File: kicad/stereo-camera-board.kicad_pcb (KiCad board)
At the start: 4 copper layers, 57 x 70 mm, 86 parts, among them IC1 ZLDO1117G33TA, IC2 MCP1700T-2502E/TT, IC3 SN74LVC1T45DCKR, IC4 SN74LVC1T45DCKR, IC5 SN74LVC1T45DCKR, T1 2n2222a, T2 2N2907A, U1 GSB311231HR, U2 ATXMEGA256A3-AU, U3 MAX3207E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

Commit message: Cleaned up module references for silk screen.
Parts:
- FSM4JSMA-SMD: renamed from Reset; value FSM4JSMA-SMD -> RESET
- JP3: value AVR-JTAG-10 -> JTAG
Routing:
- net N-0000067: track 14.9 -> 16.2 mm
- net (no net): track 1.19 -> 1.29 mm, vias 0 -> 109
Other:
- board text added: "+5V"
- board text added: "GND"

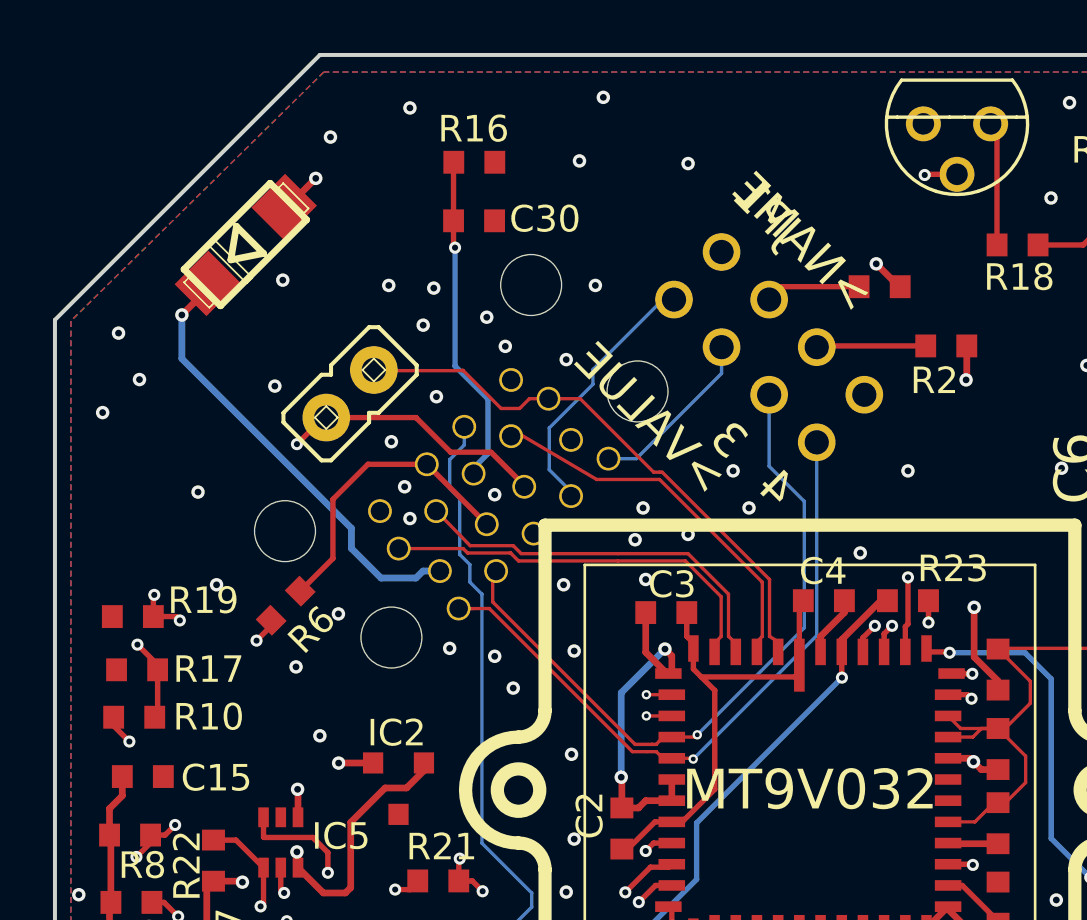
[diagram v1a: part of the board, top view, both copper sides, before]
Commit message: Modified usb module
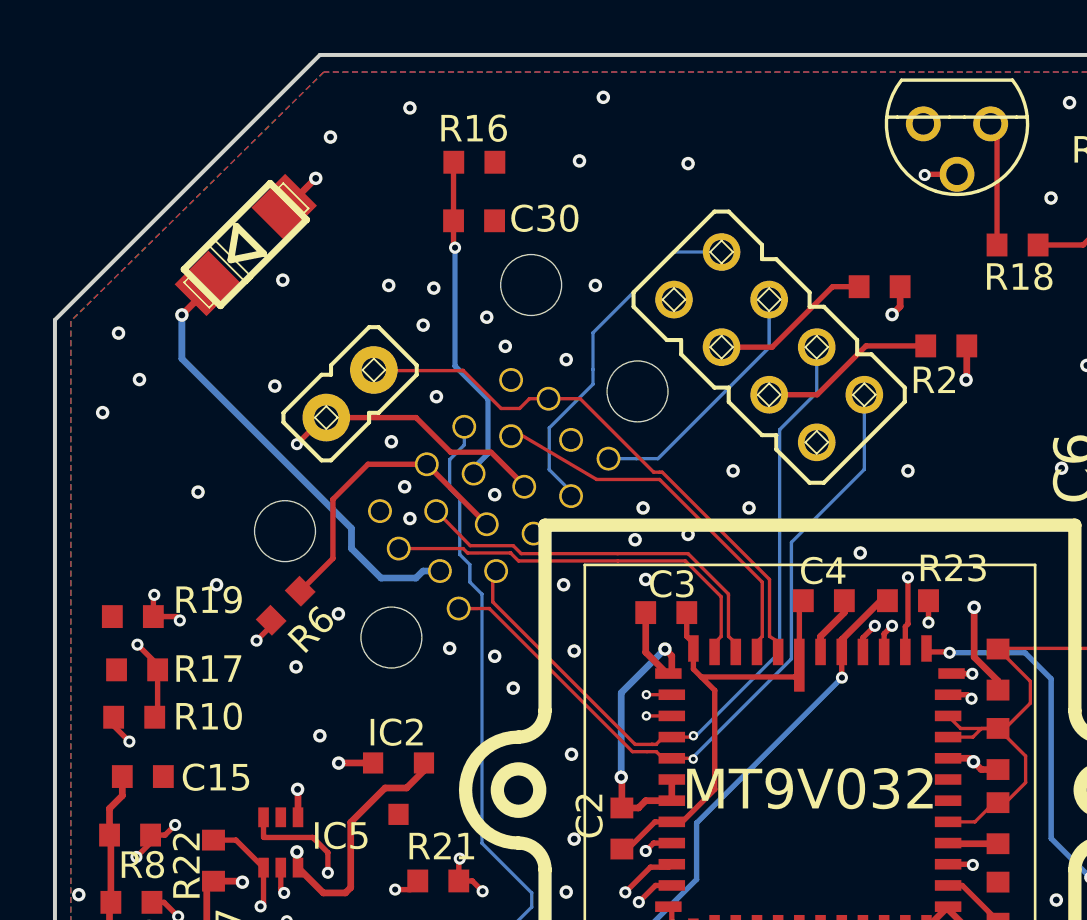
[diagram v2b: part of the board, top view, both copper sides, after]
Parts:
- JP1: moved to F.Cu
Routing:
- net N-0000084: track 20.0 -> 23.3 mm
- net N-0000083: track 16.6 -> 19.6 mm
- net N-0000025: track 3.60 -> 6.14 mm
- net N-0000063: track 4.13 -> 6.67 mm
- net N-0000086: track 24.7 -> 27.2 mm
- net N-0000085: track 26.0 -> 27.5 mm

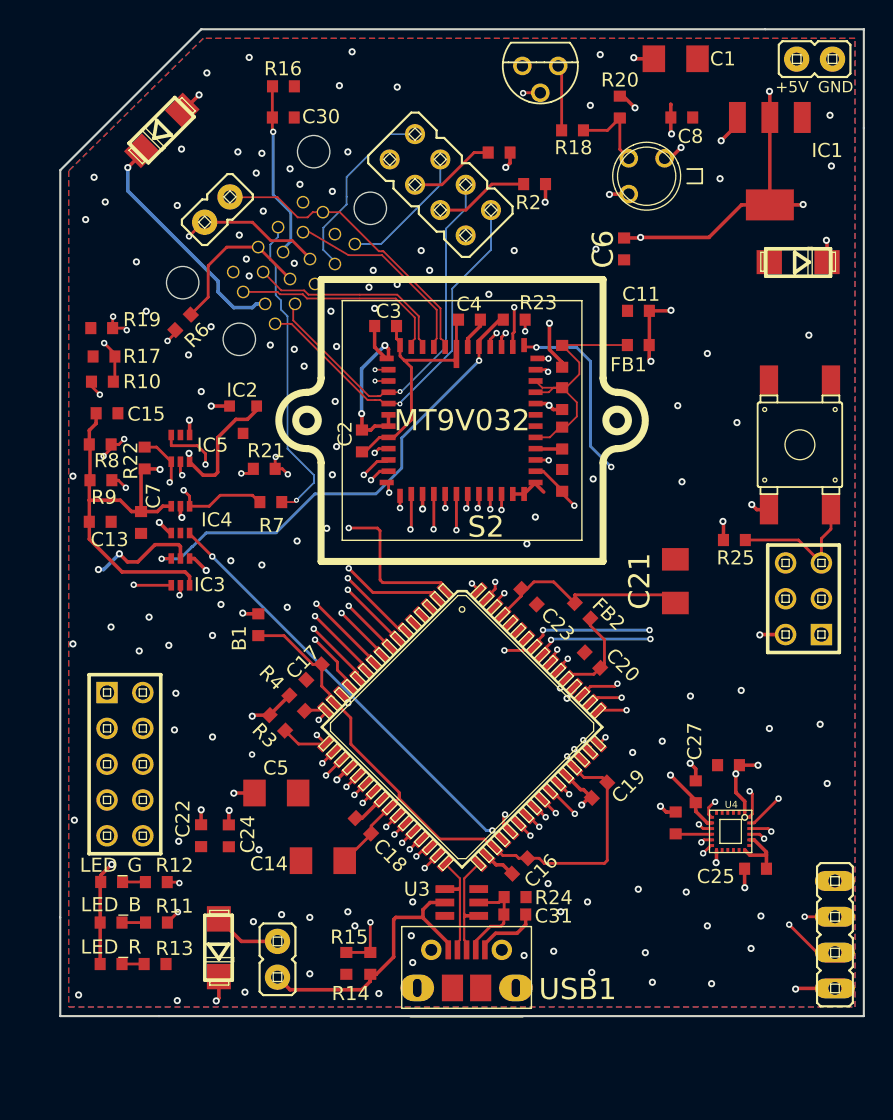
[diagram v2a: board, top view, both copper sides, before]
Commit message: Removed plane-to-plane vias as Kicad does not support them well. Added shield pins to micro usb in schematic. Updated netlist in PcbNew and fixed pins in micro usb to match new shield pins.
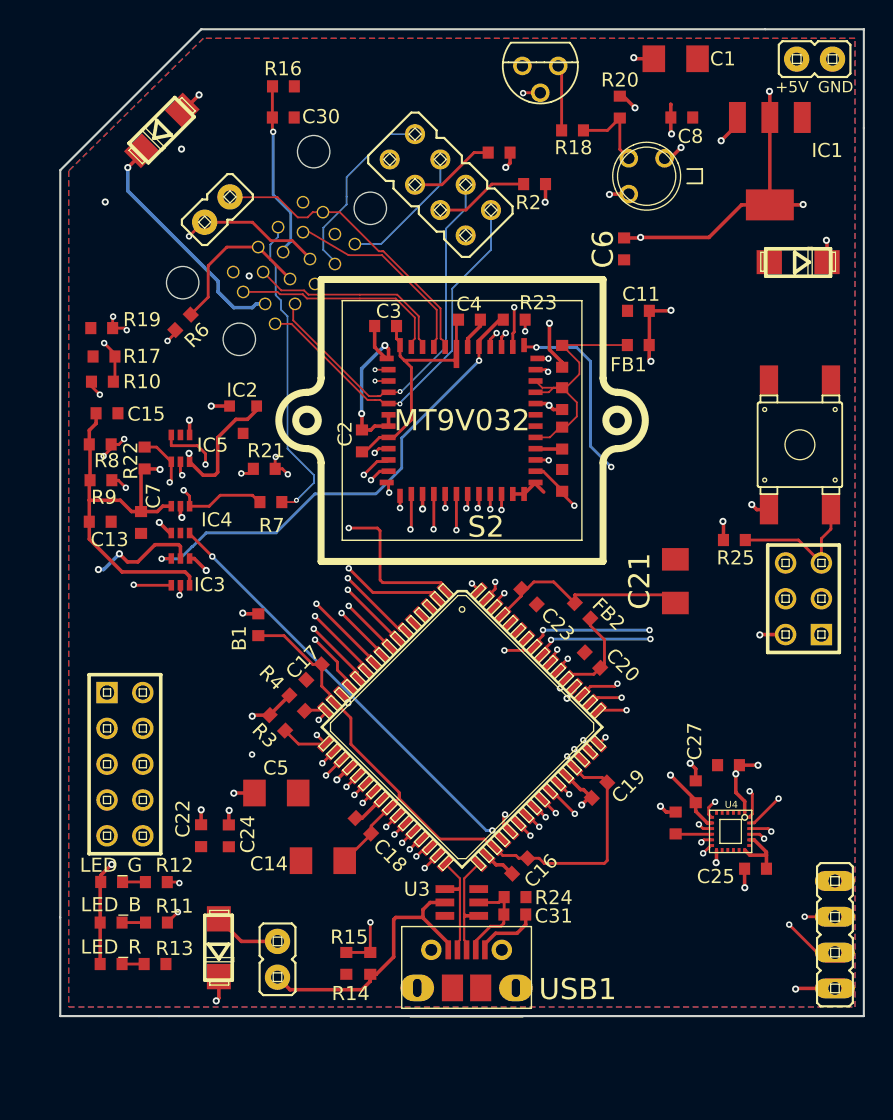
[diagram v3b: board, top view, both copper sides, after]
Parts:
- JP3: value JTAG -> AVR-JTAG-10
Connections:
- C31 pad 2: N-0000051 -> Net-(C31-Pad2)
- JP3 pad 6: N-0000090 -> Net-(JP3-Pad6)
- R24 pad 1: N-0000051 -> Net-(C31-Pad2)
- R25 pad 1: N-0000090 -> Net-(JP3-Pad6)
- U2 pad 56: N-0000016 -> Net-(PDIJTAG1-Pad1)
- U2 pad 57: N-0000090 -> Net-(JP3-Pad6)
- U3 pad 2: N-0000051 -> Net-(C31-Pad2)
- USB1 pad 11: (no net) -> Net-(C31-Pad2)
- USB1 pad 4: N-0000051 -> Net-(USB1-Pad4)
- USB1 pad 6: (no net) -> Net-(C31-Pad2)
- USB1 pad 8: (no net) -> Net-(C31-Pad2)
- USB1 pad 9: (no net) -> Net-(C31-Pad2)
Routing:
- net N-0000090: track 64.8 -> 28.5 mm, vias 4 -> 2
- net Net-(JP3-Pad6): track 0.00 -> 36.3 mm, vias 0 -> 2
- net N-0000051: track 6.96 -> 0.00 mm
- net Net-(C31-Pad2): track 0.00 -> 4.85 mm
- net Net-(USB1-Pad4): track 0.00 -> 2.11 mm
- net N-0000016: track 21.3 -> 20.3 mm
- net Net-(PDIJTAG1-Pad1): track 0.00 -> 1.07 mm
- net (no net): vias 109 -> 2

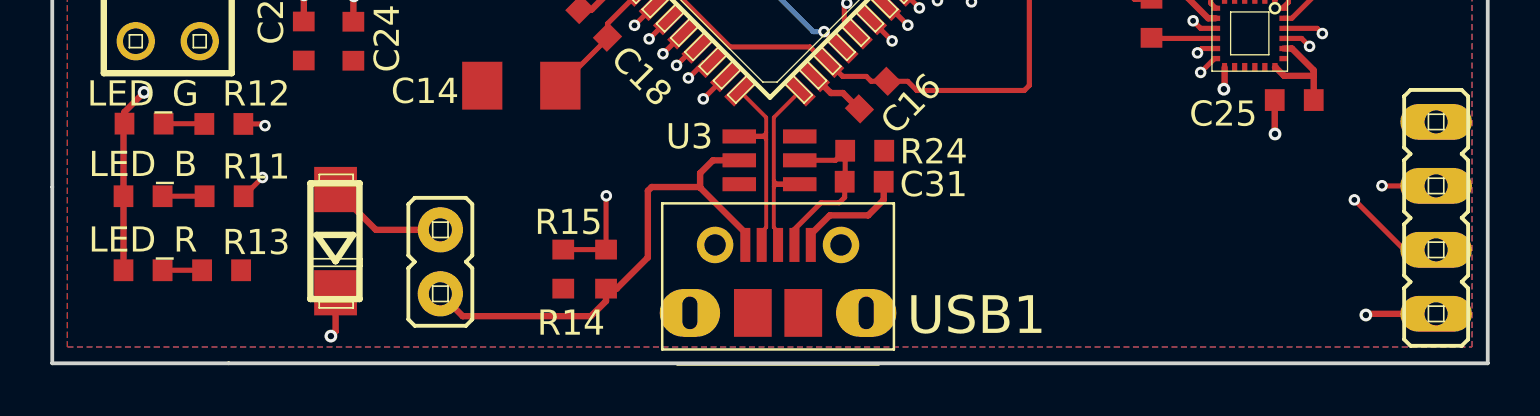
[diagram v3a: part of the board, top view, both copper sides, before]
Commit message: Connected shield on USB connector.
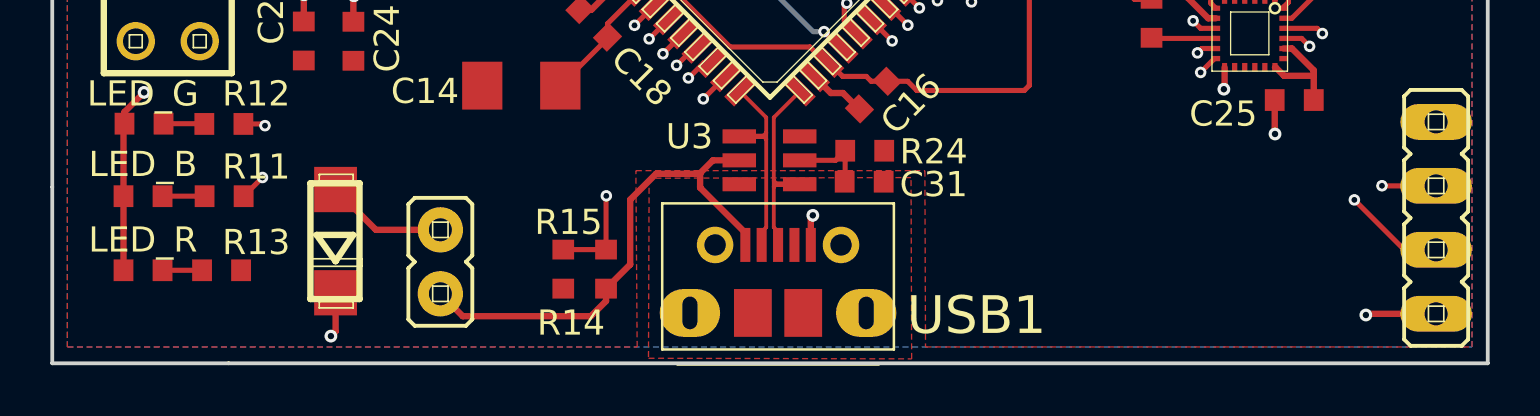
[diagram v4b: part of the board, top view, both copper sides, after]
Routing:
- net GND: track 56.9 -> 53.9 mm, vias 12 -> 13
- net Net-(USB1-Pad4): track 2.11 -> 0.00 mm
- net Net-(C31-Pad2): track 4.85 -> 3.20 mm
- added copper zone on F.Cu, net Net-(C31-Pad2)

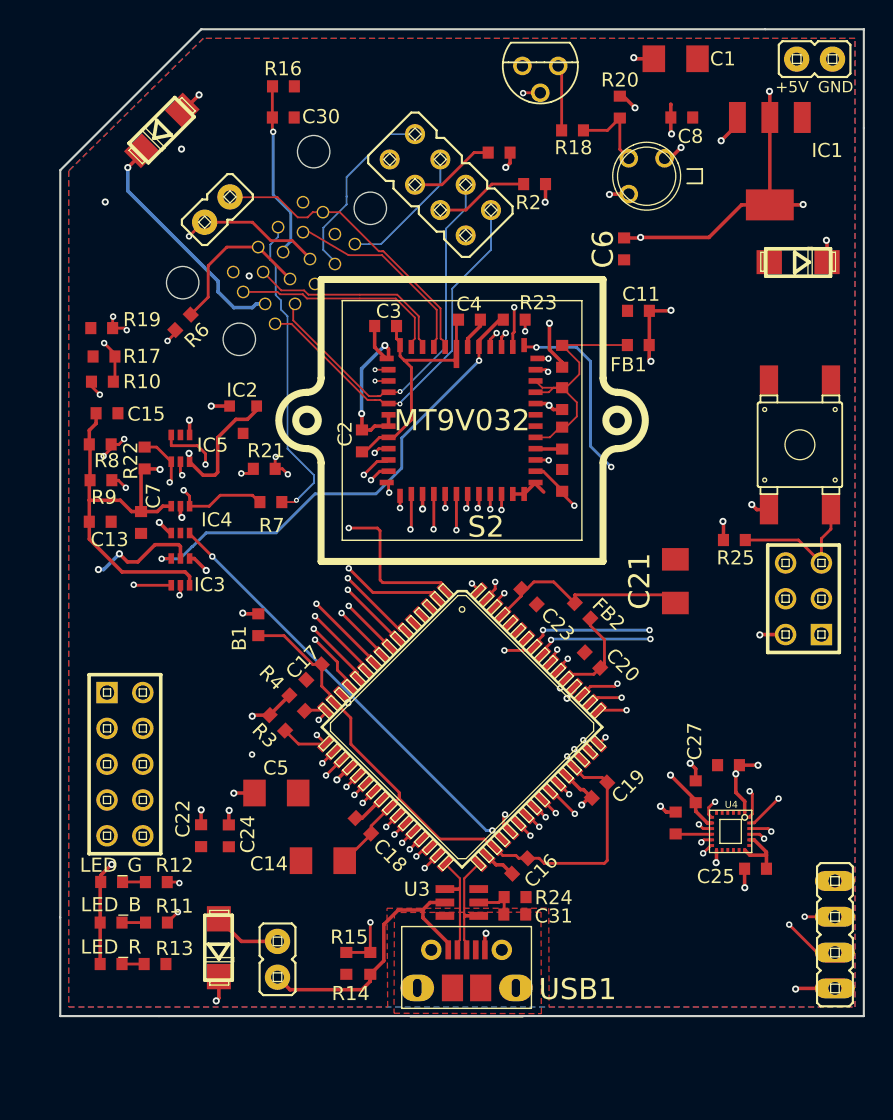
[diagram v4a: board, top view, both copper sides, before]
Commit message: Added via module and placed it around the board
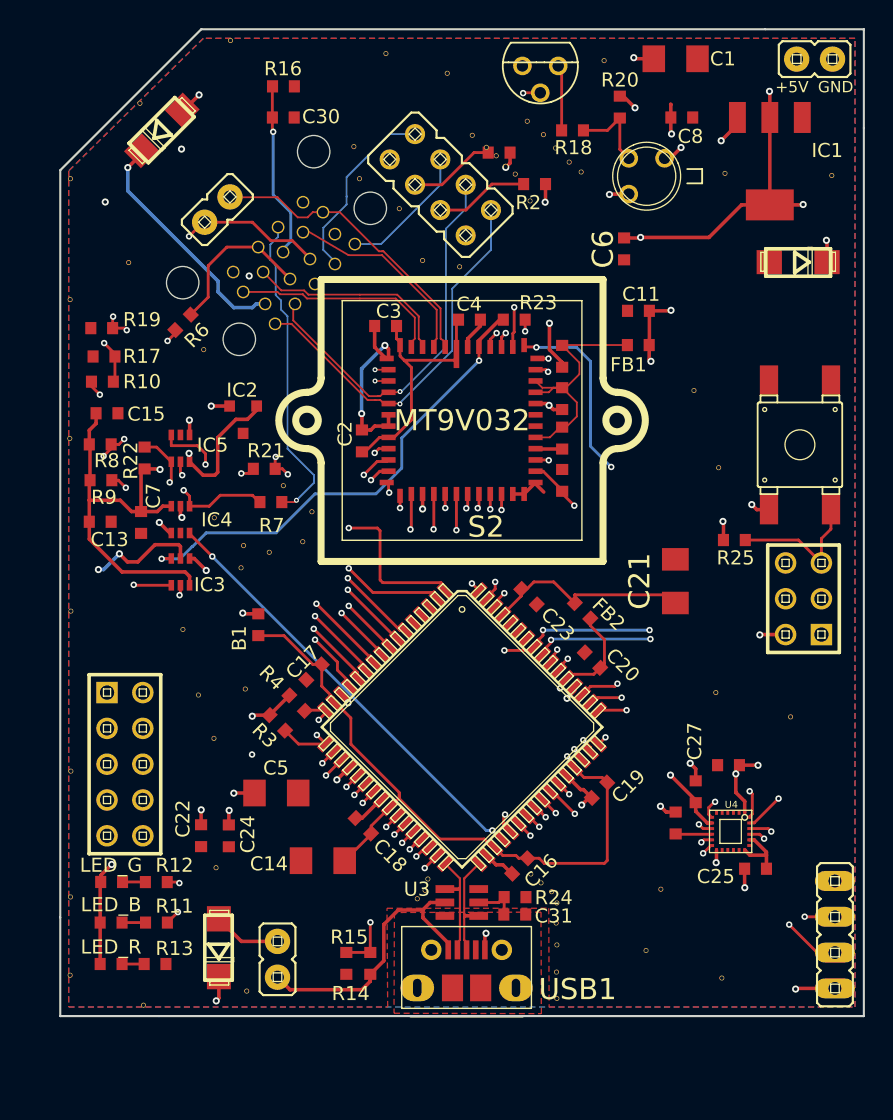
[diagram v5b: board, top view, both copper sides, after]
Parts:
- added Via5Mil: VAL**, ViasAndHoles:Via5Mil, F.Cu at (133.2, 148.2)
- added Via5Mil: VAL**, ViasAndHoles:Via5Mil, F.Cu at (125.7, 85.2)
- added Via5Mil: VAL**, ViasAndHoles:Via5Mil, F.Cu at (132.1, 80.8)
- added Via5Mil: VAL**, ViasAndHoles:Via5Mil, F.Cu at (147.4, 83.1)
- added Via5Mil: VAL**, ViasAndHoles:Via5Mil, F.Cu at (167.2, 90.2)
- added Via5Mil: VAL**, ViasAndHoles:Via5Mil, F.Cu at (153.1, 86.5)
- added Via5Mil: VAL**, ViasAndHoles:Via5Mil, F.Cu at (154.3, 87.5)
- added Via5Mil: VAL**, ViasAndHoles:Via5Mil, F.Cu at (155.1, 88.4)
- added Via5Mil: VAL**, ViasAndHoles:Via5Mil, F.Cu at (156.1, 89.4)
- added Via5Mil: VAL**, ViasAndHoles:Via5Mil, F.Cu at (156.9, 90.1)
- added Via5Mil: VAL**, ViasAndHoles:Via5Mil, F.Cu at (149.2, 87.5)
- added Via5Mil: VAL**, ViasAndHoles:Via5Mil, F.Cu at (125.9, 149.2)
- added Via5Mil: VAL**, ViasAndHoles:Via5Mil, F.Cu at (150.2, 88.4)
- added Via5Mil: VAL**, ViasAndHoles:Via5Mil, F.Cu at (150.9, 89.0)
- added Via5Mil: VAL**, ViasAndHoles:Via5Mil, F.Cu at (151.6, 89.7)
- added Via5Mil: VAL**, ViasAndHoles:Via5Mil, F.Cu at (152.3, 90.3)
- added Via5Mil: VAL**, ViasAndHoles:Via5Mil, F.Cu at (153.3, 92.2)
- added Via5Mil: VAL**, ViasAndHoles:Via5Mil, F.Cu at (164.9, 105.6)
- added Via5Mil: VAL**, ViasAndHoles:Via5Mil, F.Cu at (166.5, 127.0)
- added Via5Mil: VAL**, ViasAndHoles:Via5Mil, F.Cu at (155.2, 148.8)
- added Via5Mil: VAL**, ViasAndHoles:Via5Mil, F.Cu at (155.2, 146.9)
- added Via5Mil: VAL**, ViasAndHoles:Via5Mil, F.Cu at (155.2, 144.9)
- added Via5Mil: VAL**, ViasAndHoles:Via5Mil, F.Cu at (120.7, 147.1)
- added Via5Mil: VAL**, ViasAndHoles:Via5Mil, F.Cu at (155.2, 143.4)
- added Via5Mil: VAL**, ViasAndHoles:Via5Mil, F.Cu at (155.2, 142.0)
- added Via5Mil: VAL**, ViasAndHoles:Via5Mil, F.Cu at (154.8, 141.2)
- added Via5Mil: VAL**, ViasAndHoles:Via5Mil, F.Cu at (154.1, 140.6)
- added Via5Mil: VAL**, ViasAndHoles:Via5Mil, F.Cu at (153.4, 139.9)
- added Via5Mil: VAL**, ViasAndHoles:Via5Mil, F.Cu at (146.1, 140.3)
- added Via5Mil: VAL**, ViasAndHoles:Via5Mil, F.Cu at (145.9, 141.1)
- added Via5Mil: VAL**, ViasAndHoles:Via5Mil, F.Cu at (145.3, 141.7)
- added Via5Mil: VAL**, ViasAndHoles:Via5Mil, F.Cu at (166.9, 147.3)
- added Via5Mil: VAL**, ViasAndHoles:Via5Mil, F.Cu at (131.1, 139.5)
- added Via5Mil: VAL**, ViasAndHoles:Via5Mil, F.Cu at (120.7, 141.6)
- added Via5Mil: VAL**, ViasAndHoles:Via5Mil, F.Cu at (130.9, 130.3)
- added Via5Mil: VAL**, ViasAndHoles:Via5Mil, F.Cu at (129.8, 127.2)
- added Via5Mil: VAL**, ViasAndHoles:Via5Mil, F.Cu at (133.1, 126.8)
- added Via5Mil: VAL**, ViasAndHoles:Via5Mil, F.Cu at (128.7, 122.6)
- added Via5Mil: VAL**, ViasAndHoles:Via5Mil, F.Cu at (132.8, 118.2)
- added Via5Mil: VAL**, ViasAndHoles:Via5Mil, F.Cu at (130.9, 114.7)
- added Via5Mil: VAL**, ViasAndHoles:Via5Mil, F.Cu at (133.0, 116.6)
- added Via5Mil: VAL**, ViasAndHoles:Via5Mil, F.Cu at (137.2, 116.3)
- added Via5Mil: VAL**, ViasAndHoles:Via5Mil, F.Cu at (134.8, 117.1)
- added Via5Mil: VAL**, ViasAndHoles:Via5Mil, F.Cu at (135.8, 112.4)
- added Via5Mil: VAL**, ViasAndHoles:Via5Mil, F.Cu at (120.8, 132.6)
- added Via5Mil: VAL**, ViasAndHoles:Via5Mil, F.Cu at (137.8, 114.2)
- added Via5Mil: VAL**, ViasAndHoles:Via5Mil, F.Cu at (161.6, 145.3)
- added Via5Mil: VAL**, ViasAndHoles:Via5Mil, F.Cu at (162.6, 141.0)
- added Via5Mil: VAL**, ViasAndHoles:Via5Mil, F.Cu at (171.8, 128.8)
- added Via5Mil: VAL**, ViasAndHoles:Via5Mil, F.Cu at (166.7, 111.1)
- added Via5Mil: VAL**, ViasAndHoles:Via5Mil, F.Cu at (174.7, 90.4)
- added Via5Mil: VAL**, ViasAndHoles:Via5Mil, F.Cu at (158.6, 82.2)
- added Via5Mil: VAL**, ViasAndHoles:Via5Mil, F.Cu at (143.1, 81.7)
- added Via5Mil: VAL**, ViasAndHoles:Via5Mil, F.Cu at (140.8, 88.3)
- added Via5Mil: VAL**, ViasAndHoles:Via5Mil, F.Cu at (124.8, 96.5)
- added Via5Mil: VAL**, ViasAndHoles:Via5Mil, F.Cu at (120.8, 121.3)
- added Via5Mil: VAL**, ViasAndHoles:Via5Mil, F.Cu at (145.7, 96.4)
- added Via5Mil: VAL**, ViasAndHoles:Via5Mil, F.Cu at (148.3, 96.8)
- added Via5Mil: VAL**, ViasAndHoles:Via5Mil, F.Cu at (141.2, 90.6)
- added Via5Mil: VAL**, ViasAndHoles:Via5Mil, F.Cu at (144.1, 92.7)
- added Via5Mil: VAL**, ViasAndHoles:Via5Mil, F.Cu at (130.2, 102.7)
- added Via5Mil: VAL**, ViasAndHoles:Via5Mil, F.Cu at (120.7, 109.0)
- added Via5Mil: VAL**, ViasAndHoles:Via5Mil, F.Cu at (120.7, 99.2)
- added Via5Mil: VAL**, ViasAndHoles:Via5Mil, F.Cu at (120.7, 90.6)
